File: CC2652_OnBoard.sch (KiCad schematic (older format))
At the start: 28 parts, among them IC1 CC2652R1FRGZR

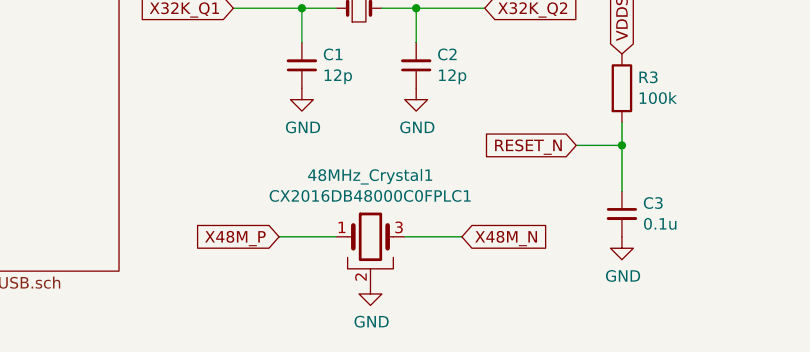
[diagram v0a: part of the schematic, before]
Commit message: Agregar PNGS
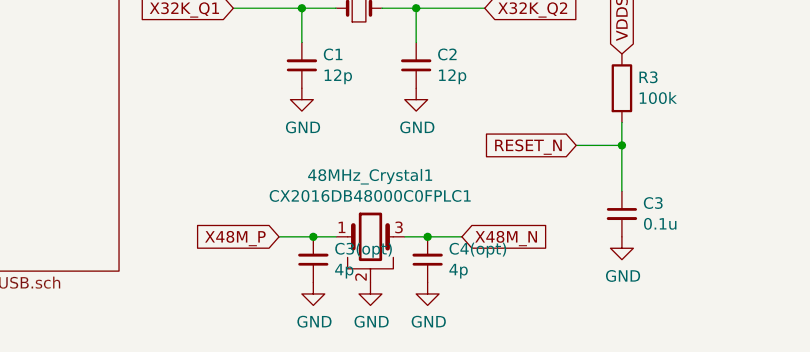
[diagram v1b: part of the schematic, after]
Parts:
- added C3(opt), C4(opt): 4p, Capacitor_SMD:C_0402_1005Metric, symbol Device:C_Small
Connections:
- net GND: now also C3(opt).1, C4(opt).1
- net X48M_N: now also C4(opt).2
- net X48M_P: now also C3(opt).2
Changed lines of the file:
@@
 $EndComp
 Wire Wire Line
-	3300 7200 3050 7200
+	3300 7200 3150 7200
 Text GLabel 3300 7200 2    50   Input ~ 0
 X48M_N
@@
 X48M_P
 Wire Wire Line
-	2500 7200 2750 7200
+	2500 7200 2650 7200
 $Comp
 L power:GND #PWR0111
@@
 F1 "Perifericos.sch" 50
 $EndSheet
+$Comp
+L Device:C_Small C3(opt)
+U 1 1 6129B392
+P 2650 7300
+F 0 "C3(opt)" H 2558 7254 50  0000 R CNN
+F 1 "4p" H 2558 7345 50  0000 R CNN
+F 2 "Capacitor_SMD:C_0402_1005Metric" H 2650 7300 50  0001 C CNN
+F 3 "https://www.mouser.ca/c/?q=grm1555" H 2650 7300 50  0001 C CNN
+	1    2650 7300
+	-1   0    0    1
+$EndComp
+Connection ~ 2650 7200
+Wire Wire Line
+	2650 7200 2750 7200
+$Comp
+L Device:C_Small C4(opt)
+U 1 1 6129B933
+P 3150 7300
+F 0 "C4(opt)" H 3058 7254 50  0000 R CNN
+F 1 "4p" H 3058 7345 50  0000 R CNN
+F 2 "Capacitor_SMD:C_0402_1005Metric" H 3150 7300 50  0001 C CNN
+F 3 "https://www.mouser.ca/c/?q=grm1555" H 3150 7300 50  0001 C CNN
+	1    3150 7300
+	-1   0    0    1
+$EndComp
+Connection ~ 3150 7200
+Wire Wire Line
+	3150 7200 3050 7200
+$Comp
+L power:GND #PWR?
+U 1 1 6129C0C5
+P 3150 7400
+F 0 "#PWR?" H 3150 7150 50  0001 C CNN
+F 1 "GND" H 3155 7227 50  0000 C CNN
+F 2 "" H 3150 7400 50  0001 C CNN
+F 3 "" H 3150 7400 50  0001 C CNN
+	1    3150 7400
+	1    0    0    -1
+$EndComp
+$Comp
+L power:GND #PWR?
+U 1 1 6129C4AE
+P 2650 7400
+F 0 "#PWR?" H 2650 7150 50  0001 C CNN
+F 1 "GND" H 2655 7227 50  0000 C CNN
+F 2 "" H 2650 7400 50  0001 C CNN
+F 3 "" H 2650 7400 50  0001 C CNN
+	1    2650 7400
+	1    0    0    -1
+$EndComp
 $EndSCHEMATC
